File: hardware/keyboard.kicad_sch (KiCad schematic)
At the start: 48 parts, among them SW1 SW_Push, SW10 SW_Push, SW11 SW_Push, SW12 SW_Push, SW13 SW_Push, SW14 SW_Push, SW15 SW_Push, SW16 SW_Push, SW17 SW_Push, SW18 SW_Push, SW19 SW_Push, SW2 SW_Push, SW20 SW_Push, SW21 SW_Push, SW22 SW_Push, SW23 SW_Push, SW25 SW_Push, SW26 SW_Push, SW27 SW_Push, SW28 SW_Push, SW29 SW_Push, SW3 SW_Push, SW30 SW_Push, SW31 SW_Push, SW33 SW_Push, SW34 SW_Push, SW35 SW_Push, SW36 SW_Push, SW37 SW_Push, SW38 SW_Push, SW39 SW_Push, SW4 SW_Push, SW5 SW_Push, SW58 SKRHABE010, SW6 SW_Push, SW7 SW_Push, SW9 SW_Push, U11 PCA9555PW

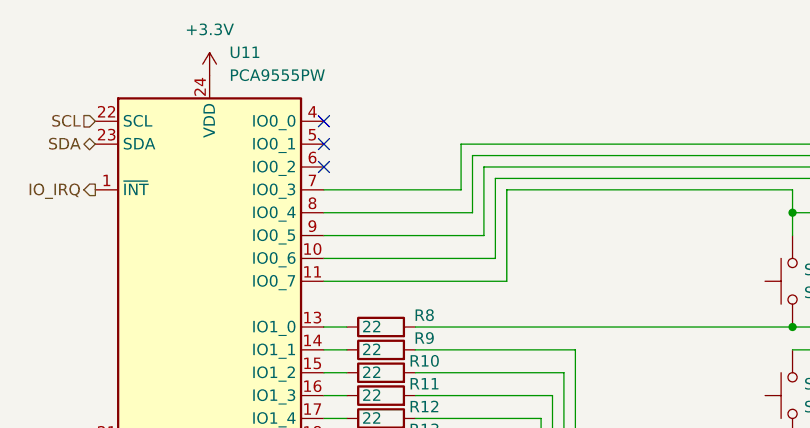
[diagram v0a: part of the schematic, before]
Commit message: Route all board
Fix CS missing for SD card
Add IMU symbol and footprint to the project lib
Finish esp32 pinswaps
Move non critical signals to the keyboard IO expander
Add power flag symbols
Fix Dpad pin type
Fix IMU pin type
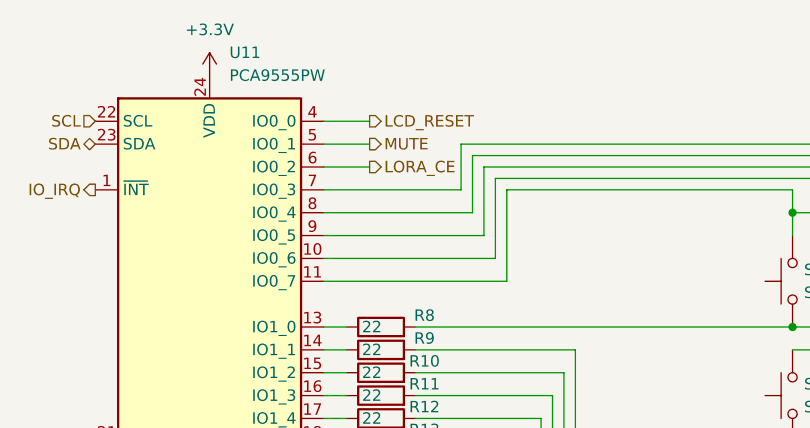
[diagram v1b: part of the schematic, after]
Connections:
- net LCD_RESET: now reaches U11.4 (IO0_0)
- net MUTE: now reaches U11.5 (IO0_1)
- net LORA_CE: now reaches U11.6 (IO0_2)
- no-connect marks 3 -> 0
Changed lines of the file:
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@@
 		(color 0 0 0 0)
 	)
-	(no_connect
-		(at 63.5 45.72)
-	)
-	(no_connect
-		(at 63.5 40.64)
-	)
-	(no_connect
-		(at 63.5 43.18)
-	)
 	(wire
 		(pts
@@
 	(wire
 		(pts
+			(xy 63.5 43.18) (xy 68.58 43.18)
+		)
+		(stroke
+			(width 0)
+			(type default)
+		)
+	)
+	(wire
+		(pts
 			(xy 200.66 50.8) (xy 196.85 50.8)
 		)
@@
 	(wire
 		(pts
+			(xy 63.5 40.64) (xy 68.58 40.64)
+		)
+		(stroke
+			(width 0)
+			(type default)
+		)
+	)
+	(wire
+		(pts
 			(xy 87.63 73.66) (xy 87.63 114.3)
 		)
@@
 		(pts
 			(xy 91.44 66.04) (xy 91.44 76.2)
+		)
+		(stroke
+			(width 0)
+			(type default)
+		)
+	)
+	(wire
+		(pts
+			(xy 63.5 45.72) (xy 68.58 45.72)
 		)
 		(stroke
@@
 		)
 	)
+	(hierarchical_label "LCD_RESET"
+		(shape output)
+		(at 68.58 40.64 0)
+		(fields_autoplaced yes)
+		(effects
+			(font
+				(size 1.27 1.27)
+			)
+			(justify left)
+		)
+	)
+	(hierarchical_label "MUTE"
+		(shape output)
+		(at 68.58 43.18 0)
+		(fields_autoplaced yes)
+		(effects
+			(font
+				(size 1.27 1.27)
+			)
+			(justify left)
+		)
+	)
+	(hierarchical_label "LORA_CE"
+		(shape output)
+		(at 68.58 45.72 0)
+		(fields_autoplaced yes)
+		(effects
+			(font
+				(size 1.27 1.27)
+			)
+			(justify left)
+		)
+	)

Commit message: Associate all LCSC component
Change sdcard pullup resistor to 47K
Center main schematic
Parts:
- C20: LCSC (none) -> C1691
- R10, R11, R12, R13, R14, R15, R8, R9: LCSC (none) -> C107701
- SW1, SW10, SW11, SW12, SW13, SW14, SW15, SW16, SW17, SW18, SW19, SW2, SW20, SW21, SW22, SW23, SW25, SW26, SW27, SW28, SW29, SW3, SW30, SW31, SW33, SW34, SW35, SW36, SW37, SW38, SW39, SW4, SW5, SW6, SW7, SW9: LCSC (none) -> C2888430
- SW58: LCSC (none) -> C139794
- U11: LCSC C128392 -> C128392

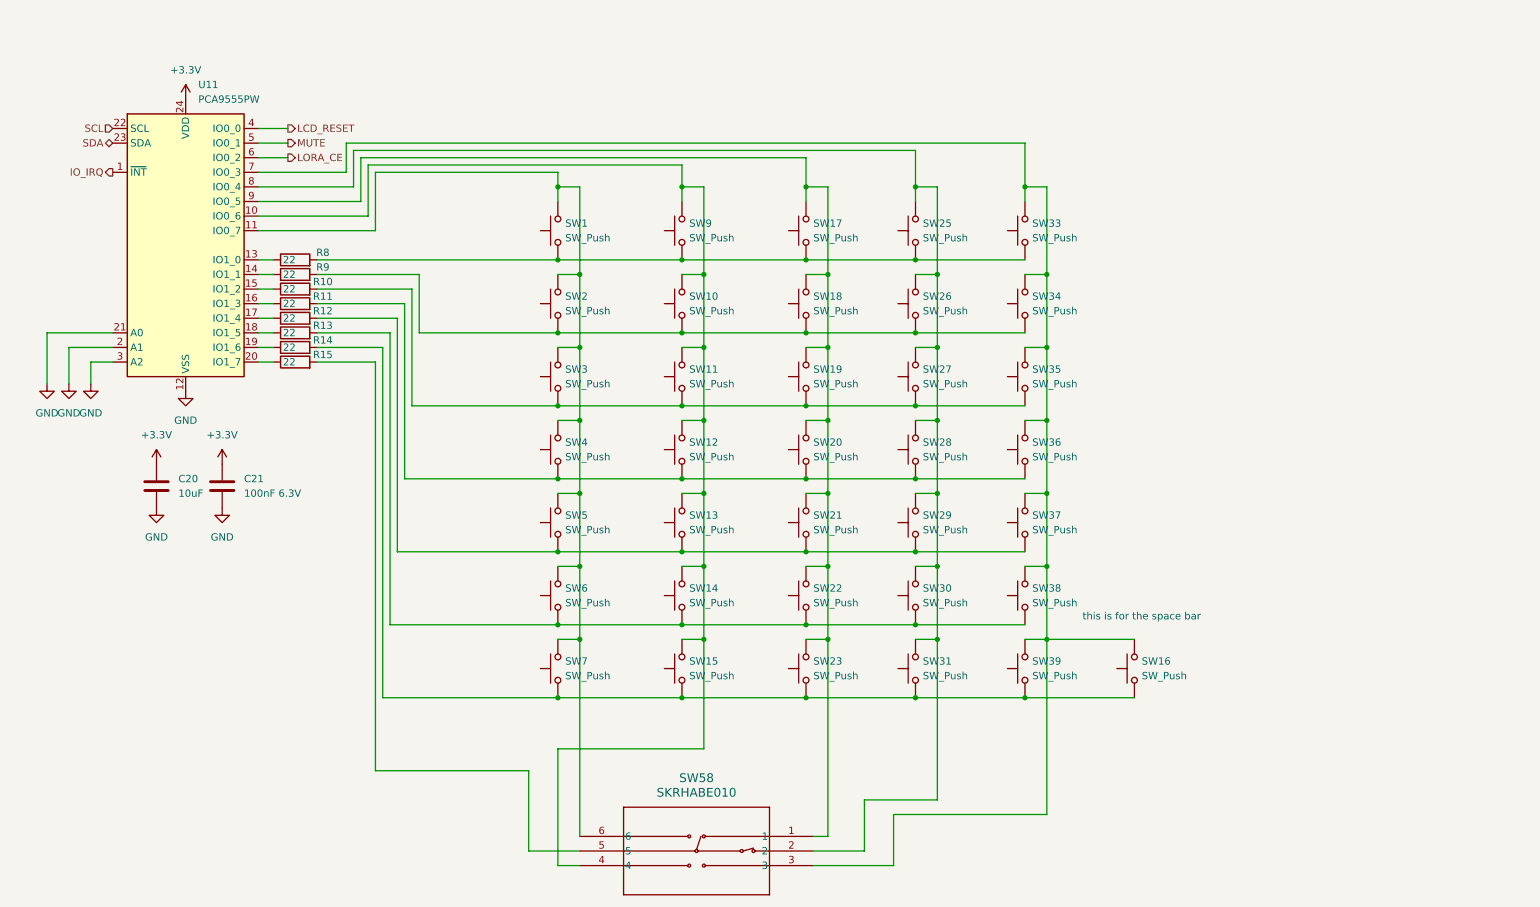
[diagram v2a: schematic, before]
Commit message: Beautified schematic, added I2C addresses
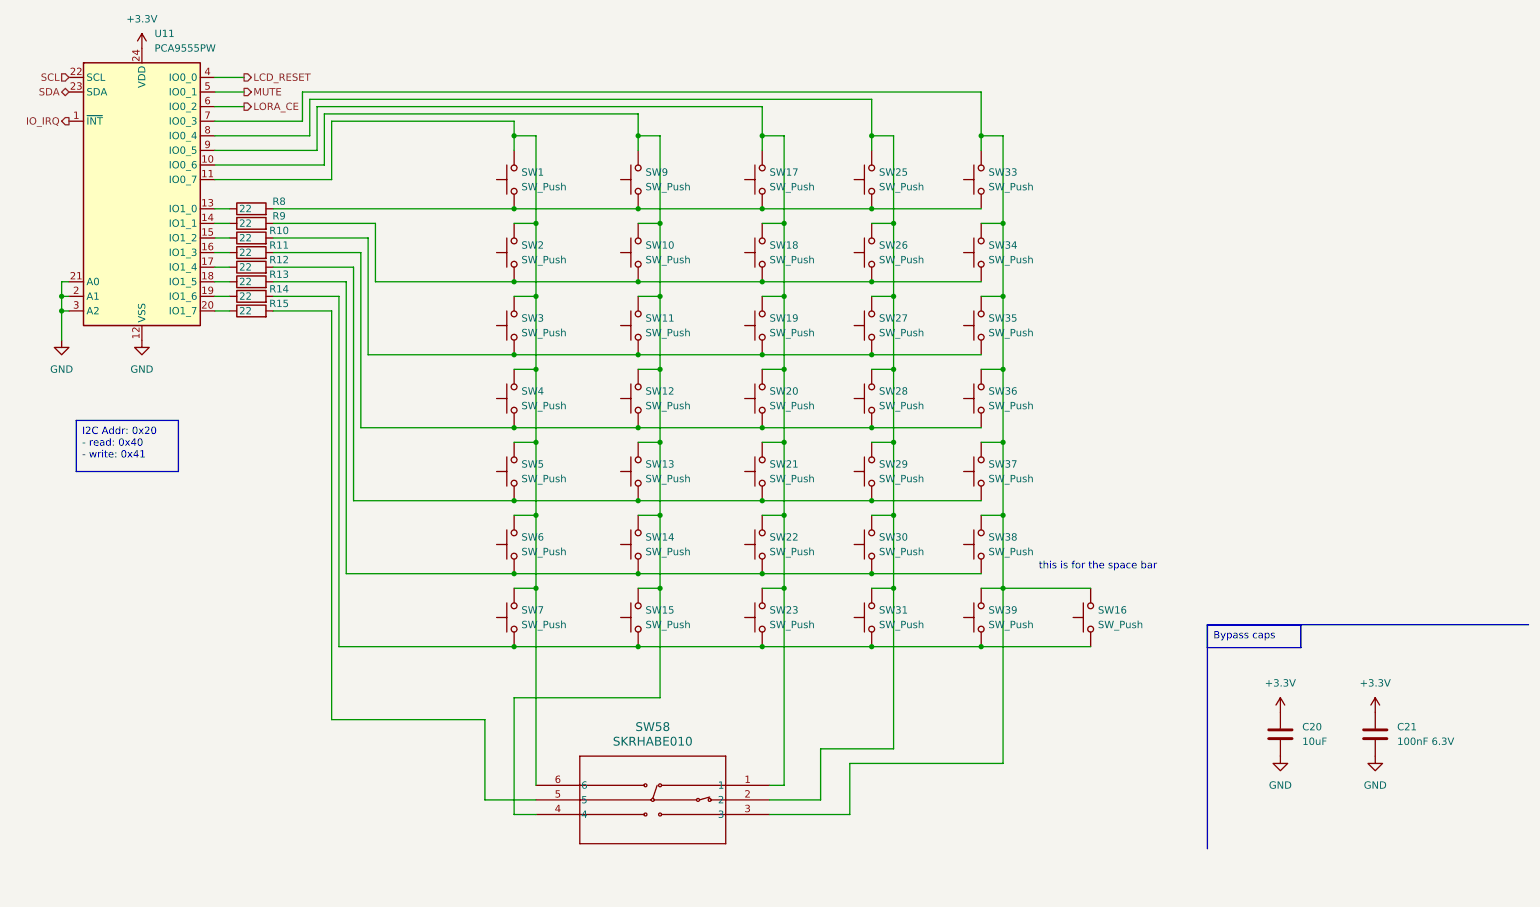
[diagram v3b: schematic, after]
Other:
- moved on the sheet: C20, C21, R10, R11, R12, R13, R14, R15, R8, R9, SW1, SW10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

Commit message: update lcsc codes to use (new?) basic components
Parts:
- C20: LCSC C1691 -> C19702
- R10, R11, R12, R13, R14, R15, R8, R9: LCSC C107701 -> C23345
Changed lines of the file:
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@@
 			)
 		)
-		(property "LCSC" "C107701"
+		(property "LCSC" "C23345"
 			(at 62.23 69.85 0)
 			(effects
@@
 			)
 		)
-		(property "LCSC" "C107701"
+		(property "LCSC" "C23345"
 			(at 62.23 57.15 0)
 			(effects
@@
 			)
 		)
-		(property "LCSC" "C107701"
+		(property "LCSC" "C23345"
 			(at 62.23 67.31 0)
 			(effects
@@
 			)
 		)
-		(property "LCSC" "C107701"
+		(property "LCSC" "C23345"
 			(at 62.23 62.23 0)
 			(effects
@@
 			)
 		)
-		(property "LCSC" "C107701"
+		(property "LCSC" "C23345"
 			(at 62.23 54.61 0)
 			(effects
@@
 			)
 		)
-		(property "LCSC" "C107701"
+		(property "LCSC" "C23345"
 			(at 62.23 64.77 0)
 			(effects
@@
 			)
 		)
-		(property "LCSC" "C107701"
+		(property "LCSC" "C23345"
 			(at 62.23 59.69 0)
 			(effects
@@
 			)
 		)
-		(property "LCSC" "C1691"
+		(property "LCSC" "C19702"
 			(at 241.3 146.05 0)
 			(effects
@@
 			)
 		)
-		(property "LCSC" "C107701"
+		(property "LCSC" "C23345"
 			(at 62.23 72.39 0)
 			(effects
